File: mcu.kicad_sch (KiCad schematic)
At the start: 19 parts, among them J1 Conn_01x04_Socket, SW1 SW_Push, SW2 SW_Push, U1 ESP32-C3-MINI-1, Y1 32.768kHz

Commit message: added test points
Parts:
- added TP3: +3v3, TestPoint:TestPoint_Pad_1.0x1.0mm, symbol Connector:TestPoint
- added TP4: GND, TestPoint:TestPoint_Pad_1.0x1.0mm, symbol Connector:TestPoint
- added TP5: SCL, TestPoint:TestPoint_Pad_1.0x1.0mm, symbol Connector:TestPoint
- added TP6: SDA, TestPoint:TestPoint_Pad_1.0x1.0mm, symbol Connector:TestPoint
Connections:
- net +3.3V: now also TP3.1
- net GND: now also TP4.1
- net SCL: now also TP5.1
- net SDA: now also TP6.1
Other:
- moved on the sheet: J1

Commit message: Made changes up to diode logic
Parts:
- C5: value 10uF -> 0.1uF; footprint Capacitor_SMD:C_0805_2012Metric_Pad1.18x1.45mm_HandSolder -> Capacitor_SMD:C_0603_1608Metric_Pad1.08x0.95mm_HandSolder
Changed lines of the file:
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@@
 			)
 		)
-		(property "Value" "10uF"
+		(property "Value" "0.1uF"
 			(at 133.35 59.6962 0)
 			(effects
@@
 			)
 		)
-		(property "Footprint" "Capacitor_SMD:C_0805_2012Metric_Pad1.18x1.45mm_HandSolder"
+		(property "Footprint" "Capacitor_SMD:C_0603_1608Metric_Pad1.08x0.95mm_HandSolder"
 			(at 130.81 58.42 0)
 			(effects

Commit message: made remaining changes to the schematic
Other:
- moved on the sheet: TP3, TP4
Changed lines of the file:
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@@
 	(wire
 		(pts
-			(xy 251.46 35.56) (xy 251.46 38.1)
+			(xy 241.3 36.83) (xy 241.3 39.37)
 		)
 		(stroke
@@
 	(wire
 		(pts
-			(xy 251.46 27.94) (xy 254 27.94)
+			(xy 241.3 29.21) (xy 243.84 29.21)
 		)
 		(stroke
@@
 	(wire
 		(pts
-			(xy 251.46 35.56) (xy 254 35.56)
+			(xy 241.3 36.83) (xy 243.84 36.83)
 		)
 		(stroke
@@
 	(wire
 		(pts
-			(xy 251.46 25.4) (xy 251.46 27.94)
+			(xy 241.3 26.67) (xy 241.3 29.21)
 		)
 		(stroke
@@
 	(symbol
 		(lib_id "Connector:TestPoint")
-		(at 254 27.94 270)
+		(at 243.84 29.21 270)
 		(unit 1)
 		(exclude_from_sim no)
@@
 		(fields_autoplaced yes)
 		(property "Reference" "TP3"
-			(at 259.08 26.6699 90)
+			(at 248.92 27.9399 90)
 			(effects
 				(font
@@
 		)
 		(property "Value" "+3v3"
-			(at 259.08 29.2099 90)
+			(at 248.92 30.4799 90)
 			(effects
 				(font
@@
 		)
 		(property "Footprint" "TestPoint:TestPoint_Pad_1.0x1.0mm"
-			(at 254 33.02 0)
+			(at 243.84 34.29 0)
 			(effects
 				(font
@@
 		)
 		(property "Datasheet" "~"
-			(at 254 33.02 0)
+			(at 243.84 34.29 0)
 			(effects
 				(font
@@
 		)
 		(property "Description" "test point"
-			(at 254 27.94 0)
+			(at 243.84 29.21 0)
 			(effects
 				(font
@@
 	(symbol
 		(lib_id "power:GND")
-		(at 251.46 38.1 0)
+		(at 241.3 39.37 0)
 		(unit 1)
 		(exclude_from_sim no)
@@
 		(fields_autoplaced yes)
 		(property "Reference" "#PWR052"
-			(at 251.46 44.45 0)
+			(at 241.3 45.72 0)
 			(effects
 				(font
@@
 		)
 		(property "Value" "GND"
-			(at 251.46 43.18 0)
+			(at 241.3 44.45 0)
 			(effects
 				(font
@@
 		)
 		(property "Footprint" ""
-			(at 251.46 38.1 0)
+			(at 241.3 39.37 0)
 			(effects
 				(font
@@
 		)
 		(property "Datasheet" ""
-			(at 251.46 38.1 0)
+			(at 241.3 39.37 0)
 			(effects
 				(font
@@
 		)
 		(property "Description" "Power symbol creates a global label with name \"GND\" , ground"
-			(at 251.46 38.1 0)
+			(at 241.3 39.37 0)
 			(effects
 				(font
@@
 	(symbol
 		(lib_id "power:+3.3V")
-		(at 251.46 25.4 0)
+		(at 241.3 26.67 0)
 		(unit 1)
 		(exclude_from_sim no)
@@
 		(fields_autoplaced yes)
 		(property "Reference" "#PWR051"
-			(at 251.46 29.21 0)
+			(at 241.3 30.48 0)
 			(effects
 				(font
@@
 		)
 		(property "Value" "+3.3V"
-			(at 251.46 20.32 0)
+			(at 241.3 21.59 0)
 			(effects
 				(font
@@
 		)
 		(property "Footprint" ""
-			(at 251.46 25.4 0)
+			(at 241.3 26.67 0)
 			(effects
 				(font
@@
 		)
 		(property "Datasheet" ""
-			(at 251.46 25.4 0)
+			(at 241.3 26.67 0)
 			(effects
 				(font
@@
 		)
 		(property "Description" "Power symbol creates a global label with name \"+3.3V\""
-			(at 251.46 25.4 0)
+			(at 241.3 26.67 0)
 			(effects
 				(font
@@
 	(symbol
 		(lib_id "Connector:TestPoint")
-		(at 254 35.56 270)
+		(at 243.84 36.83 270)
 		(unit 1)
 		(exclude_from_sim no)
@@
 		(fields_autoplaced yes)
 		(property "Reference" "TP4"
-			(at 259.08 34.2899 90)
+			(at 248.92 35.5599 90)
 			(effects
 				(font
@@
 		)
 		(property "Value" "GND"
-			(at 259.08 36.8299 90)
+			(at 248.92 38.0999 90)
 			(effects
 				(font
@@
 		)
 		(property "Footprint" "TestPoint:TestPoint_Pad_1.0x1.0mm"
-			(at 254 40.64 0)
+			(at 243.84 41.91 0)
 			(effects
 				(font
@@
 		)
 		(property "Datasheet" "~"
-			(at 254 40.64 0)
+			(at 243.84 41.91 0)
 			(effects
 				(font
@@
 		)
 		(property "Description" "test point"
-			(at 254 35.56 0)
+			(at 243.84 36.83 0)
 			(effects
 				(font

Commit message: addressed Craig's comments
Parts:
- removed D1: IN-S126TASRGB, bookbuddy:LED_IN-S126TASRGB, symbol IN-S126TASRGB:IN-S126TASRGB
- added C4: DNP, Capacitor_SMD:C_0805_2012Metric_Pad1.18x1.45mm_HandSolder, symbol Device:C_Small
- added LED1: IN-S63TBS5R5G5B, IN-S63TBS5R5G5B_INO, symbol IN_S63TBS5R5G5B:IN-S63TBS5R5G5B
- J1: value Conn_01x04_Socket -> SM04B-SRSS-TB; footprint bookbuddy:GCT_BC075-04-A-L-A_REVC2 -> bookbuddy:CONN_SM04B-SRSS-TB_JST
- R5: value 27 -> 240
- R6: value 27 -> 39
- R7: value 91 -> 39
- renumbered C4 to C6, C6 to C7, TP5 to TP1, TP6 to TP2
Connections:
- net +3.3V: now also C4.1, LED1.2
- net B_LED: now also R7.1; no longer R5.1
- net CHG_STAT: now also R6.1; no longer R7.1
- net GND: now also C4.2
- net G_LED: now also R5.1; no longer R6.1
- net at R5.2: now also LED1.4
- net at R7.2: now also LED1.1
- net at R6.2: now also LED1.3
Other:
- note added: "Using JST-SH 1.0mm for space with an adapter to the 2.54mm pitch male pins"
- moved on the sheet: C6, R5, R6, R7

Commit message: Added fuse
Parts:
- LED1: footprint IN-S63TBS5R5G5B_INO -> bookbuddy:IN-S63TBS5R5G5B_INO
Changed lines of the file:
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@@
 			)
 		)
-		(property "Footprint" "IN-S63TBS5R5G5B_INO"
+		(property "Footprint" "bookbuddy:IN-S63TBS5R5G5B_INO"
 			(at 259.08 124.46 0)
 			(effects

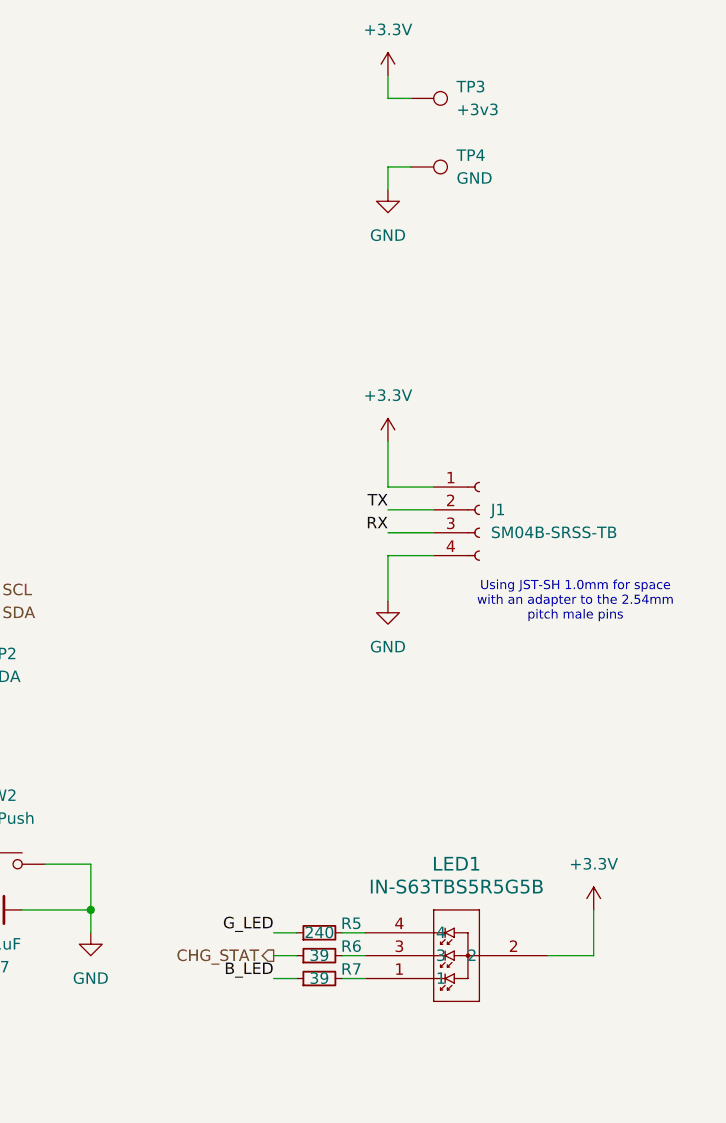
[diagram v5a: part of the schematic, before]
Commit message: switched to 4 layer
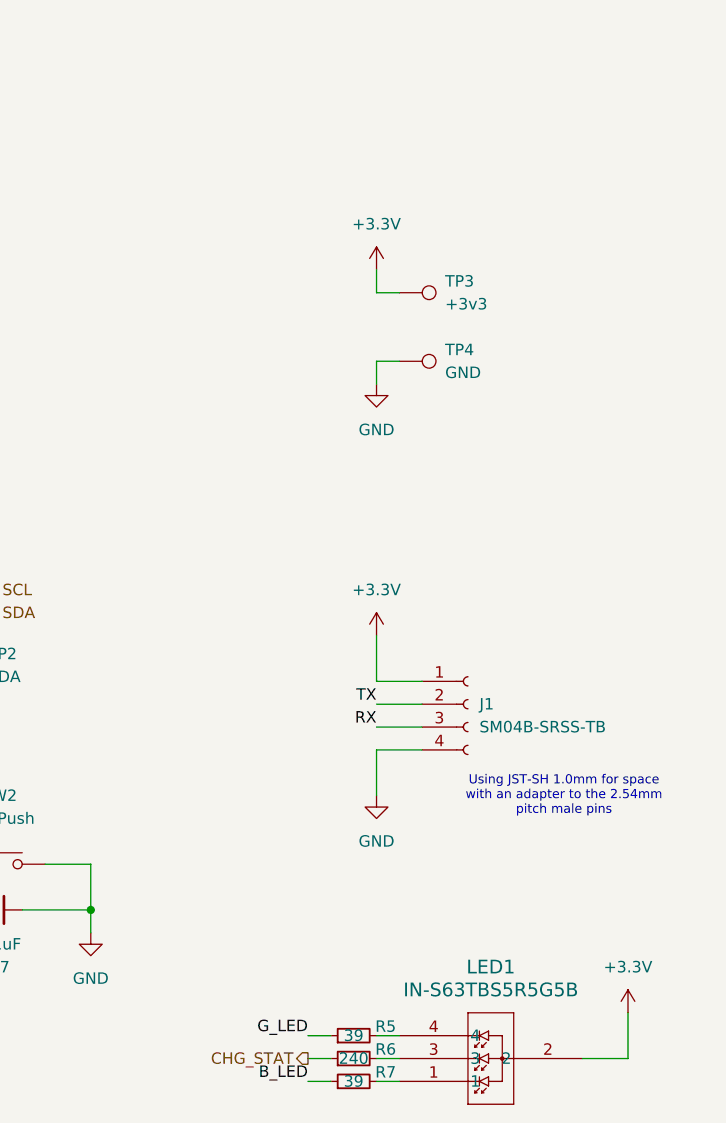
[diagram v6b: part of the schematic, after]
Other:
- moved on the sheet: J1, LED1, R5, R6, R7, TP3, TP4
